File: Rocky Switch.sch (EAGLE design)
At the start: 17 parts, among them T1 2SC1815, T2 2SC1815, T3 C1815

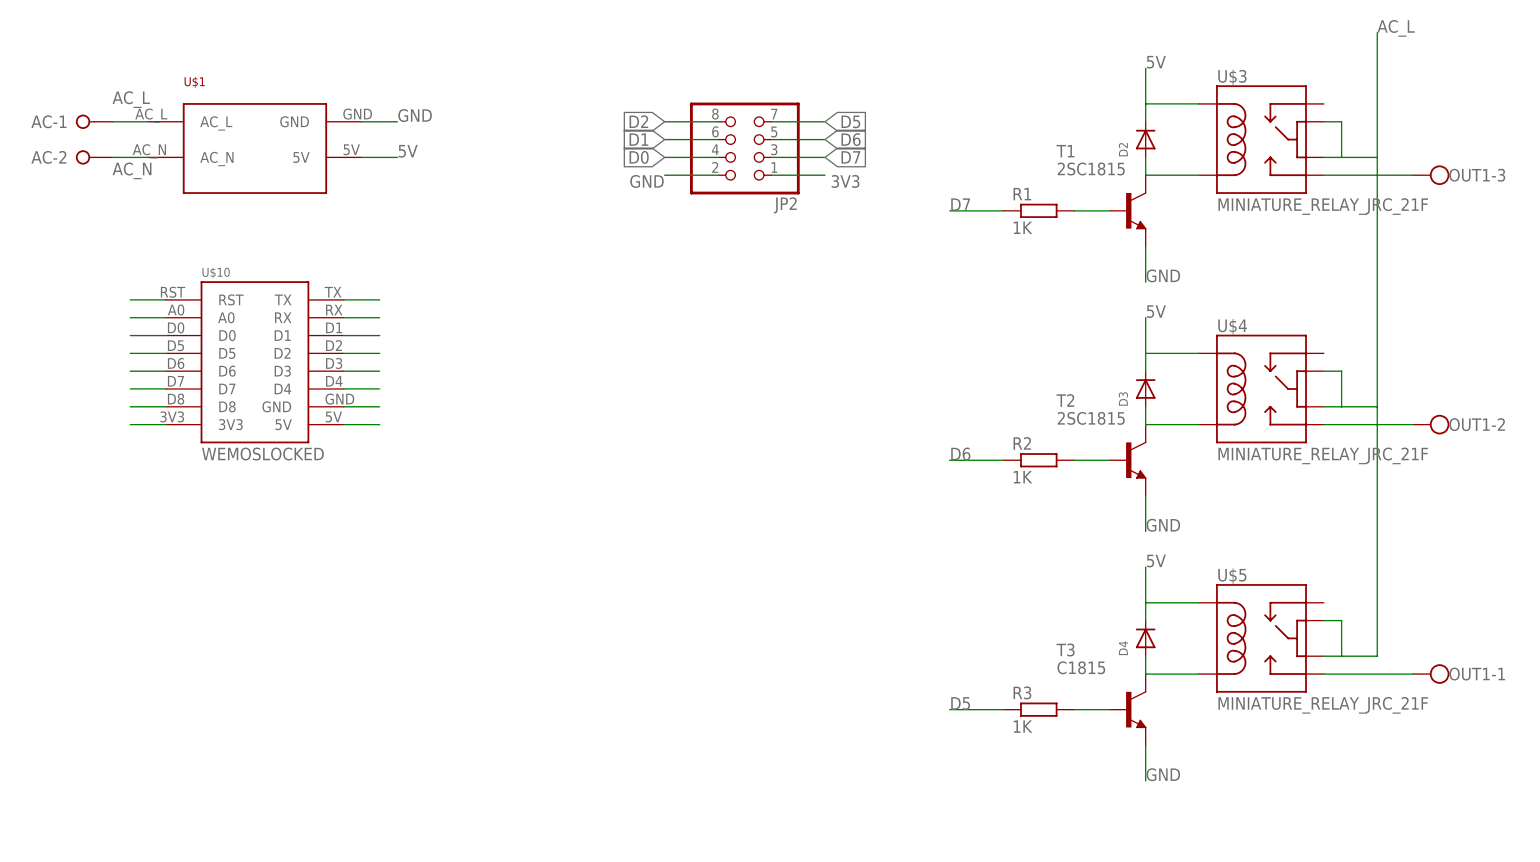
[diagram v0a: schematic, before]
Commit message: Update to new version to back to use SSR instead of mechanical relays
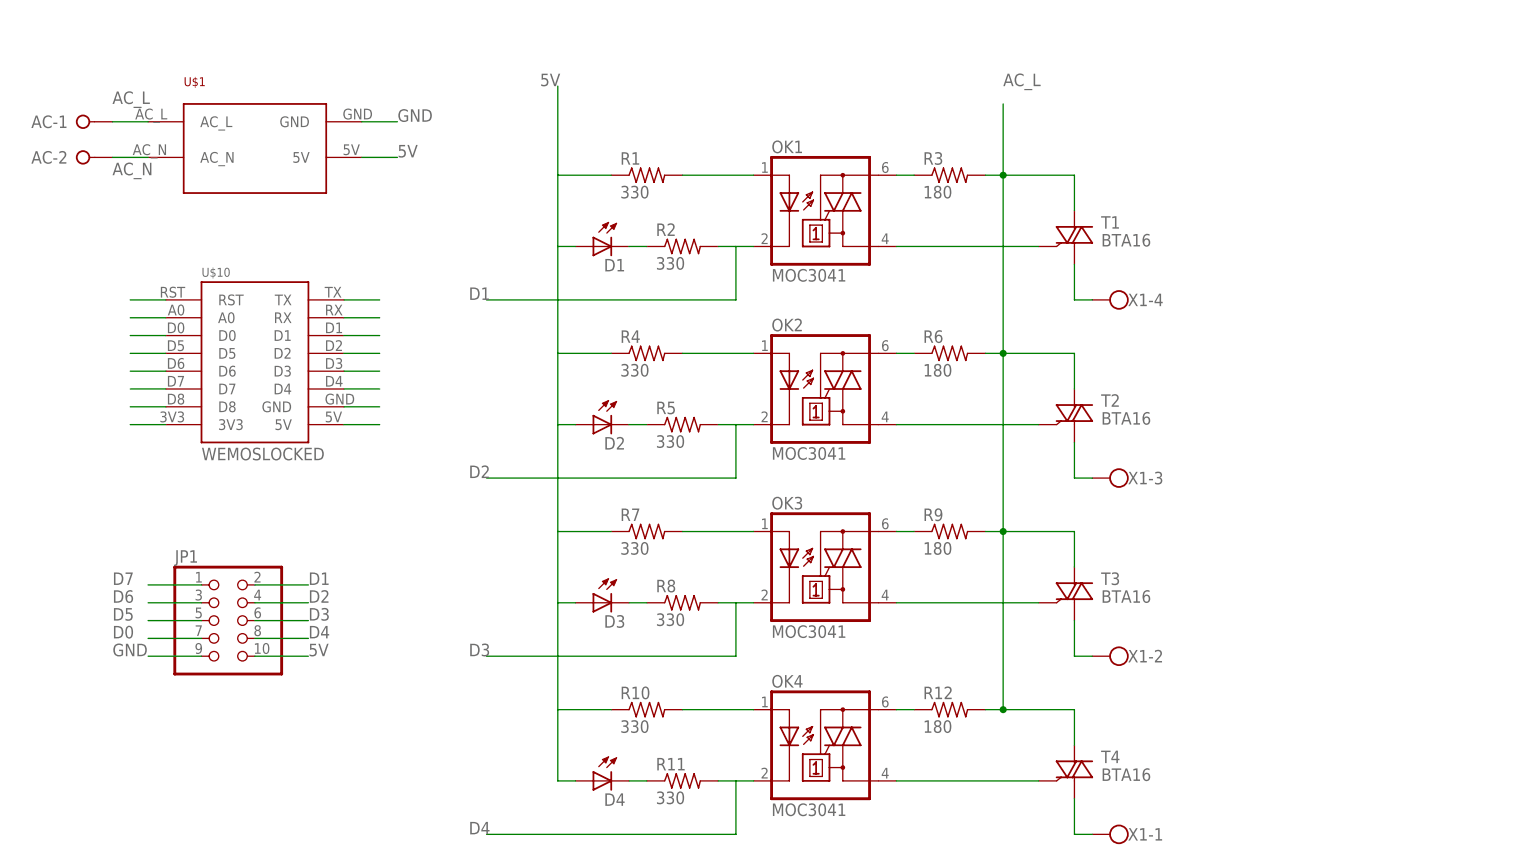
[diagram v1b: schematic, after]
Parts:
- removed JP2: (no value), adafruit:PINHD-2X4
- removed OUT1: (no value), con-wago-500:W237-103
- removed U$3, U$4, U$5: MINIATURE_RELAY_JRC_21F, My Eagle Lib:MINIATURE_RELAY_JRC_21F
- added D1: (no value), led:LED3MM
- added JP1: (no value), pinhead:PINHD-2X5
- added OK1, OK2, OK3, OK4: MOC3041, optocoupler:MOC3032T
- added R10, R11, R4, R5, R7, R8: 330, rcl:R-US_0204/7
- added R12, R6, R9: 180, rcl:R-US_0204/7
- added T4: BTA16, triac:BT138-V
- added X1: (no value), con-wago-500:W237-4
- D2, D3, D4: device adafruit:DIODESMA -> led:LED3MM
- R1, R2: value 1K -> 330; device rcl:R-EU_R0805 -> rcl:R-US_0204/7
- R3: value 1K -> 180; device rcl:R-EU_R0805 -> rcl:R-US_0204/7
- T1, T2: value 2SC1815 -> BTA16; device transistor:2SC1815 -> triac:BT138-V
- T3: value C1815 -> BTA16; device transistor:2SC1815 -> triac:BT138-V
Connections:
- removed net N$1: D2.A, T1.C, U$3.COIL2
- removed net N$11: OUT1-1.KL, U$5.NO
- removed net N$12: OUT1-2.KL, U$4.NO
- removed net N$3: D3.A, T2.C, U$4.COIL2
- removed net N$4: D4.A, T3.C, U$5.COIL2
- removed net N$5: R3.2, T3.B
- removed net N$6: R2.2, T2.B
- removed net N$7: R1.2, T1.B
- removed net N$8: OUT1-3.KL, U$3.NO
- new net N$10: OK1.A, R1.2
- new net N$14: OK1.A2, R3.1
- new net N$15: OK2.A1, T2.G
- new net N$16: OK2.A, R4.2
- new net N$17: OK2.A2, R6.1
- new net N$18: OK3.A1, T3.G
- new net N$19: OK3.A, R7.2
- new net N$20: OK3.A2, R9.1
- new net N$21: T3.A1, X1-2.KL
- new net N$22: T2.A1, X1-3.KL
- new net N$23: T1.A1, X1-4.KL
- new net N$28: D1.C, R2.1
- new net N$29: D2.C, R5.1
- new net N$30: D3.C, R8.1
- new net N$32: OK4.A1, T4.G
- new net N$33: OK4.A, R10.2
- new net N$34: OK4.A2, R12.1
- new net N$35: T4.A1, X1-1.KL
- new net N$38: D4.C, R11.1
- new net N$9: OK1.A1, T1.G
- net 3V3: no longer JP2.1
- net 5V: now also D1.A, D2.A, D3.A, D4.A, JP1.10, R1.1, R10.1, R4.1, R7.1; no longer D2.C, D3.C, D4.C, U$3.COIL1, U$4.COIL1, U$5.COIL1
- net AC_L: now also R12.2, R3.2, R6.2, R9.2, T1.A2, T2.A2, T3.A2, T4.A2; no longer U$3.COM1, U$3.COM2, U$4.COM1, U$4.COM2, U$5.COM1, U$5.COM2
- net D0: now also JP1.7; no longer JP2.4
- net D1: now also JP1.2, OK1.C, R2.2; no longer JP2.6
- net D2: now also JP1.4, OK2.C, R5.2; no longer JP2.8
- net D3: now also JP1.6, OK3.C, R8.2
- net D4: now also JP1.8, OK4.C, R11.2
- net D5: now also JP1.5; no longer JP2.7, R3.1
- net D6: now also JP1.3; no longer JP2.5, R2.1
- net D7: now also JP1.1; no longer JP2.3, R1.1
- net GND: now also JP1.9; no longer JP2.2, T1.E, T2.E, T3.E

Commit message: Update board design to version 0.2
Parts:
- removed OK1, OK2, OK3, OK4: MOC3041, optocoupler:MOC3032T
- added U1, U2, U3, U4: MOC3041, SparkFun-DiscreteSemi:MOC3031-M
- D1: value (none) -> Relay1; device led:LED3MM -> adafruit:LEDCHIP-LED0805
- D2: value (none) -> Relay2; device led:LED3MM -> adafruit:LEDCHIP-LED0805
- D3: value (none) -> Relay3; device led:LED3MM -> adafruit:LEDCHIP-LED0805
- D4: value (none) -> Relay4; device led:LED3MM -> adafruit:LEDCHIP-LED0805
- R1, R10, R11, R12, R2, R3, R4, R5, R6, R7, R8, R9: device rcl:R-US_0204/7 -> rcl:R-US_R0805
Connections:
- net D1: now also U1.2; no longer OK1.C
- net D2: now also U2.2; no longer OK2.C
- net D3: now also U3.2; no longer OK3.C
- net D4: now also U4.2; no longer OK4.C
- net N$10: now also U1.1; no longer OK1.A
- net N$14: now also U1.6; no longer OK1.A2
- net N$15: now also U2.4; no longer OK2.A1
- net N$16: now also U2.1; no longer OK2.A
- net N$17: now also U2.6; no longer OK2.A2
- net N$18: now also U3.4; no longer OK3.A1
- net N$19: now also U3.1; no longer OK3.A
- net N$20: now also U3.6; no longer OK3.A2
- net N$32: now also U4.4; no longer OK4.A1
- net N$33: now also U4.1; no longer OK4.A
- net N$34: now also U4.6; no longer OK4.A2
- net N$9: now also U1.4; no longer OK1.A1
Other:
- note added: "2016-10-08 http://easytech.vn"
- note added: "Power"
- note added: "Relays"
- note added: "Rocky Switchboard V0.2"
- note added: "Wemos D1 Mini"
- moved on the sheet: AC-1, AC-2, D1, D2, D3, D4, JP1, R1, R10, R11, R12, R2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

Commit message: Update design to version 0.3
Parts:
- R12, R3, R6, R9: device rcl:R-US_R0805 -> rcl:R-US_0204/7
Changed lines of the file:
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@@
 <part name="U$1" library="My Eagle Lib" deviceset="POWER_SUPPLY_220VAC_5V" device=""/>
 <part name="U$10" library="My Eagle Lib" deviceset="WEMOS" device="LOCKED"/>
-<part name="R3" library="rcl" deviceset="R-US_" device="R0805" value="180"/>
+<part name="R3" library="rcl" deviceset="R-US_" device="0204/7" value="180"/>
 <part name="R1" library="rcl" deviceset="R-US_" device="R0805" value="330"/>
-<part name="R6" library="rcl" deviceset="R-US_" device="R0805" value="180"/>
+<part name="R6" library="rcl" deviceset="R-US_" device="0204/7" value="180"/>
 <part name="R4" library="rcl" deviceset="R-US_" device="R0805" value="330"/>
-<part name="R9" library="rcl" deviceset="R-US_" device="R0805" value="180"/>
+<part name="R9" library="rcl" deviceset="R-US_" device="0204/7" value="180"/>
 <part name="R7" library="rcl" deviceset="R-US_" device="R0805" value="330"/>
 <part name="D1" library="adafruit" deviceset="LED" device="CHIP-LED0805" value="Relay1"/>
@@
 <part name="R5" library="rcl" deviceset="R-US_" device="R0805" value="330"/>
 <part name="R8" library="rcl" deviceset="R-US_" device="R0805" value="330"/>
-<part name="R12" library="rcl" deviceset="R-US_" device="R0805" value="180"/>
+<part name="R12" library="rcl" deviceset="R-US_" device="0204/7" value="180"/>
 <part name="R10" library="rcl" deviceset="R-US_" device="R0805" value="330"/>
 <part name="D4" library="adafruit" deviceset="LED" device="CHIP-LED0805" value="Relay4"/>

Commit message: Update design to version 1.0
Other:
- note added: "2016-10-25 http://easytech.vn"
- note added: "Rocky Switchboard v1.0"
- note removed: "2016-10-08 http://easytech.vn"
- note removed: "Rocky Switchboard V0.2"
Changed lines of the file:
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@@
 <grid distance="0.1" unitdist="inch" unit="inch" style="lines" multiple="1" display="no" altdistance="0.01" altunitdist="inch" altunit="inch"/>
 <layers>
-<layer number="1" name="Top" color="4" fill="1" visible="yes" active="no"/>
-<layer number="16" name="Bottom" color="1" fill="1" visible="yes" active="no"/>
-<layer number="17" name="Pads" color="2" fill="1" visible="yes" active="no"/>
-<layer number="18" name="Vias" color="2" fill="1" visible="yes" active="no"/>
-<layer number="19" name="Unrouted" color="6" fill="1" visible="yes" active="no"/>
-<layer number="20" name="Dimension" color="15" fill="1" visible="yes" active="no"/>
-<layer number="21" name="tPlace" color="7" fill="1" visible="yes" active="no"/>
-<layer number="22" name="bPlace" color="7" fill="1" visible="yes" active="no"/>
-<layer number="23" name="tOrigins" color="15" fill="1" visible="yes" active="no"/>
-<layer number="24" name="bOrigins" color="15" fill="1" visible="yes" active="no"/>
-<layer number="25" name="tNames" color="7" fill="1" visible="yes" active="no"/>
-<layer number="26" name="bNames" color="7" fill="1" visible="yes" active="no"/>
-<layer number="27" name="tValues" color="7" fill="1" visible="yes" active="no"/>
-<layer number="28" name="bValues" color="7" fill="1" visible="yes" active="no"/>
+<layer number="1" name="Top" color="4" fill="1" visible="no" active="no"/>
+<layer number="16" name="Bottom" color="1" fill="1" visible="no" active="no"/>
+<layer number="17" name="Pads" color="2" fill="1" visible="no" active="no"/>
+<layer number="18" name="Vias" color="2" fill="1" visible="no" active="no"/>
+<layer number="19" name="Unrouted" color="6" fill="1" visible="no" active="no"/>
+<layer number="20" name="Dimension" color="15" fill="1" visible="no" active="no"/>
+<layer number="21" name="tPlace" color="7" fill="1" visible="no" active="no"/>
+<layer number="22" name="bPlace" color="7" fill="1" visible="no" active="no"/>
+<layer number="23" name="tOrigins" color="15" fill="1" visible="no" active="no"/>
+<layer number="24" name="bOrigins" color="15" fill="1" visible="no" active="no"/>
+<layer number="25" name="tNames" color="7" fill="1" visible="no" active="no"/>
+<layer number="26" name="bNames" color="7" fill="1" visible="no" active="no"/>
+<layer number="27" name="tValues" color="7" fill="1" visible="no" active="no"/>
+<layer number="28" name="bValues" color="7" fill="1" visible="no" active="no"/>
 <layer number="29" name="tStop" color="7" fill="3" visible="no" active="no"/>
 <layer number="30" name="bStop" color="7" fill="6" visible="no" active="no"/>
@@
 <layer number="35" name="tGlue" color="7" fill="4" visible="no" active="no"/>
 <layer number="36" name="bGlue" color="7" fill="5" visible="no" active="no"/>
-<layer number="37" name="tTest" color="7" fill="1" visible="yes" active="no"/>
-<layer number="38" name="bTest" color="7" fill="1" visible="yes" active="no"/>
+<layer number="37" name="tTest" color="7" fill="1" visible="no" active="no"/>
+<layer number="38" name="bTest" color="7" fill="1" visible="no" active="no"/>
 <layer number="39" name="tKeepout" color="4" fill="11" visible="no" active="no"/>
 <layer number="40" name="bKeepout" color="1" fill="11" visible="no" active="no"/>
@@
 <layer number="44" name="Drills" color="7" fill="1" visible="no" active="no"/>
 <layer number="45" name="Holes" color="7" fill="1" visible="no" active="no"/>
-<layer number="46" name="Milling" color="3" fill="1" visible="yes" active="no"/>
-<layer number="47" name="Measures" color="7" fill="1" visible="yes" active="no"/>
-<layer number="48" name="Document" color="7" fill="1" visible="yes" active="no"/>
-<layer number="49" name="Reference" color="7" fill="1" visible="yes" active="no"/>
-<layer number="50" name="dxf" color="7" fill="1" visible="yes" active="no"/>
-<layer number="51" name="tDocu" color="7" fill="1" visible="yes" active="no"/>
-<layer number="52" name="bDocu" color="7" fill="1" visible="yes" active="no"/>
-<layer number="53" name="tGND_GNDA" color="7" fill="1" visible="yes" active="no"/>
-<layer number="54" name="bGND_GNDA" color="7" fill="1" visible="yes" active="no"/>
-<layer number="56" name="wert" color="7" fill="1" visible="yes" active="no"/>
-<layer number="57" name="tCAD" color="7" fill="1" visible="yes" active="no"/>
-<layer number="59" name="tCarbon" color="7" fill="1" visible="yes" active="no"/>
-<layer number="60" name="bCarbon" color="7" fill="1" visible="yes" active="no"/>
+<layer number="46" name="Milling" color="3" fill="1" visible="no" active="no"/>
+<layer number="47" name="Measures" color="7" fill="1" visible="no" active="no"/>
+<layer number="48" name="Document" color="7" fill="1" visible="no" active="no"/>
+<layer number="49" name="Reference" color="7" fill="1" visible="no" active="no"/>
+<layer number="50" name="dxf" color="7" fill="1" visible="no" active="no"/>
+<layer number="51" name="tDocu" color="7" fill="1" visible="no" active="no"/>
+<layer number="52" name="bDocu" color="7" fill="1" visible="no" active="no"/>
+<layer number="53" name="tGND_GNDA" color="7" fill="1" visible="no" active="no"/>
+<layer number="54" name="bGND_GNDA" color="7" fill="1" visible="no" active="no"/>
+<layer number="56" name="wert" color="7" fill="1" visible="no" active="no"/>
+<layer number="57" name="tCAD" color="7" fill="1" visible="no" active="no"/>
+<layer number="59" name="tCarbon" color="7" fill="1" visible="no" active="no"/>
+<layer number="60" name="bCarbon" color="7" fill="1" visible="no" active="no"/>
 <layer number="90" name="Modules" color="5" fill="1" visible="yes" active="yes"/>
 <layer number="91" name="Nets" color="2" fill="1" visible="yes" active="yes"/>
@@
 <wire x1="205.74" y1="251.46" x2="2.54" y2="251.46" width="0.1524" layer="97"/>
 <wire x1="2.54" y1="251.46" x2="2.54" y2="373.38" width="0.1524" layer="97"/>
-<text x="106.68" y="452.12" size="5.08" layer="97" font="vector" ratio="15">Rocky Switchboard V0.2</text>
-<text x="106.68" y="439.42" size="3.81" layer="97" font="vector" ratio="15">2016-10-08
+<text x="106.68" y="452.12" size="5.08" layer="97" font="vector" ratio="15">Rocky Switchboard v1.0</text>
+<text x="106.68" y="439.42" size="3.81" layer="97" font="vector" ratio="15">2016-10-25
 http://easytech.vn</text>
 <text x="5.08" y="436.88" size="3.81" layer="97" font="vector" ratio="15">Power</text>
